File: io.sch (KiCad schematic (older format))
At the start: 7 parts, among them J3 Conn_02x05_Odd_Even, J4 Conn_02x10_Odd_Even, J5 Conn_02x05_Odd_Even, U10 TXB0104PW, U7 TXB0108DQSR, U8 TXB0108DQSR, U9 TXB0108DQSR

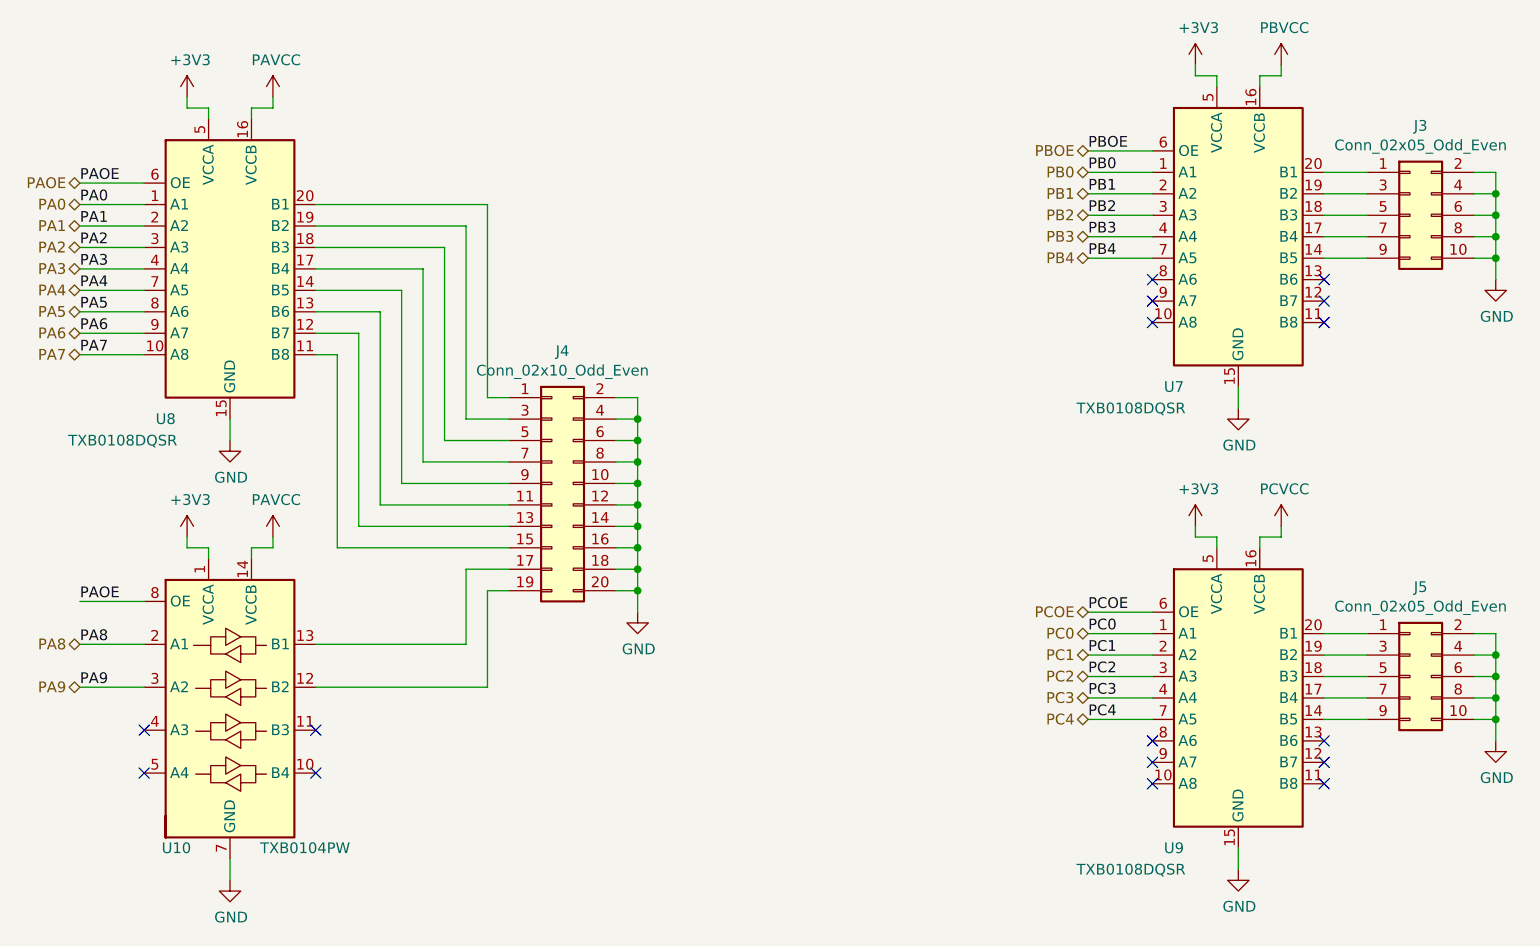
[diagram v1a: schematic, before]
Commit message: Routing should be done
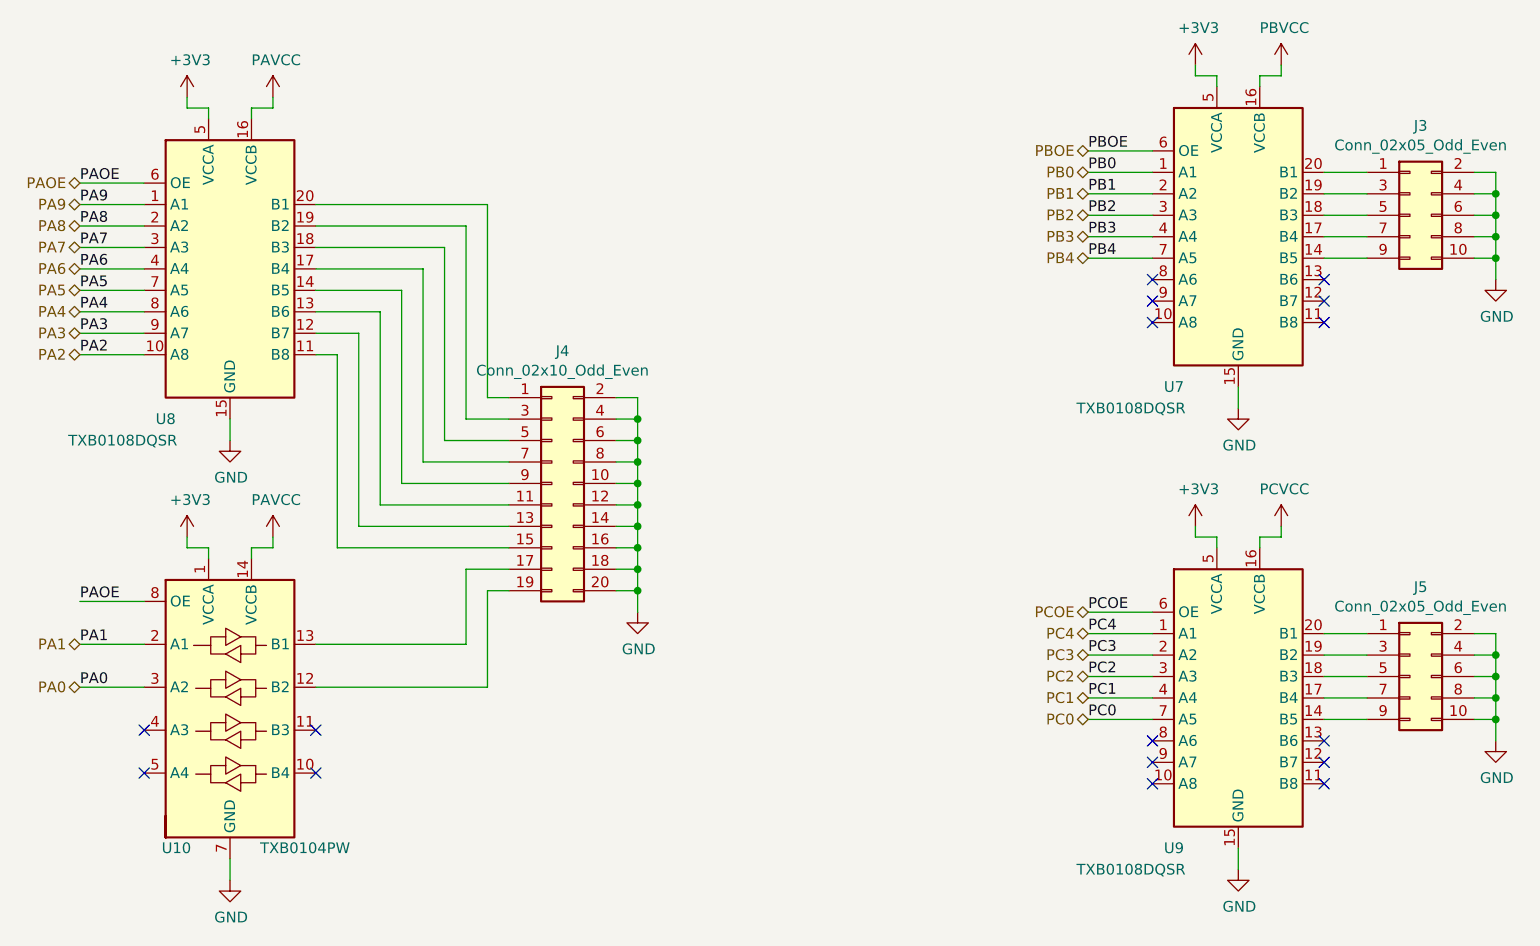
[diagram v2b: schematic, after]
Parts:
- U7, U8, U9: footprint Package_SON:USON-20_2x4mm_P0.4mm -> Package_SO:TSSOP-20_4.4x6.5mm_P0.65mm
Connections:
- net PA0: now also U10.3 (A2); no longer U8.1 (A1)
- net PA1: now also U10.2 (A1); no longer U8.2 (A2)
- net PA2: now also U8.10 (A8); no longer U8.3 (A3)
- net PA3: now also U8.9 (A7); no longer U8.4 (A4)
- net PA4: now also U8.8 (A6); no longer U8.7 (A5)
- net PA5: now also U8.7 (A5); no longer U8.8 (A6)
- net PA6: now also U8.4 (A4); no longer U8.9 (A7)
- net PA7: now also U8.3 (A3); no longer U8.10 (A8)
- net PA8: now also U8.2 (A2); no longer U10.2 (A1)
- net PA9: now also U8.1 (A1); no longer U10.3 (A2)
- net PC0: now also U9.7 (A5); no longer U9.1 (A1)
- net PC1: now also U9.4 (A4); no longer U9.2 (A2)
- net PC3: now also U9.2 (A2); no longer U9.4 (A4)
- net PC4: now also U9.1 (A1); no longer U9.7 (A5)
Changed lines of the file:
@@
-	1    0    0    -1
-$EndComp
-$Comp
-L Connector_Generic:Conn_02x10_Odd_Even J?
-U 1 1 5E95553C
-P 5300 3800
-AR Path="/5DFC2583/5E95553C" Ref="J?"  Part="1"
-AR Path="/5E933CA7/5E95553C" Ref="J4"  Part="1"
-F 0 "J4" H 5350 4417 50  0000 C CNN
-F 1 "Conn_02x10_Odd_Even" H 5350 4326 50  0000 C CNN
-F 2 "Connector_PinHeader_1.27mm:PinHeader_2x10_P1.27mm_Vertical_SMD" H 5300 3800 50  0001 C CNN
-F 3 "~" H 5300 3800 50  0001 C CNN
-	1    5300 3800
 	1    0    0    -1
 $EndComp
@@
 F 0 "U8" H 3500 2100 50  0000 C CNN
 F 1 "TXB0108DQSR" H 3300 2000 50  0000 C CNN
-F 2 "Package_SON:USON-20_2x4mm_P0.4mm" H 3800 2050 50  0001 C CNN
+F 2 "Package_SO:TSSOP-20_4.4x6.5mm_P0.65mm" H 3800 2050 50  0001 C CNN
 F 3 "http://www.ti.com/lit/ds/symlink/txb0108.pdf" H 3800 2700 50  0001 C CNN
 	1    3800 2800
@@
 F 0 "U9" H 8200 4100 50  0000 C CNN
 F 1 "TXB0108DQSR" H 8000 4000 50  0000 C CNN
-F 2 "Package_SON:USON-20_2x4mm_P0.4mm" H 8500 4050 50  0001 C CNN
+F 2 "Package_SO:TSSOP-20_4.4x6.5mm_P0.65mm" H 8500 4050 50  0001 C CNN
 F 3 "http://www.ti.com/lit/ds/symlink/txb0108.pdf" H 8500 4700 50  0001 C CNN
 	1    8500 4800
@@
 	1    0    0    -1
 $EndComp
-Text Label 3100 2500 0    50   ~ 0
+Text Label 3100 4750 0    50   ~ 0
 PA0
 Wire Wire Line
-	3400 2500 3100 2500
-Text Label 3100 2600 0    50   ~ 0
+	3400 4750 3100 4750
+Text Label 3100 4550 0    50   ~ 0
 PA1
 Wire Wire Line
-	3400 2600 3100 2600
+	3400 4550 3100 4550
+Text Label 3100 3200 0    50   ~ 0
+PA2
+Wire Wire Line
+	3400 3200 3100 3200
+Text Label 3100 3100 0    50   ~ 0
+PA3
+Wire Wire Line
+	3400 3100 3100 3100
+Text Label 3100 3000 0    50   ~ 0
+PA4
+Wire Wire Line
+	3400 3000 3100 3000
+Text Label 3100 2900 0    50   ~ 0
+PA5
+Wire Wire Line
+	3400 2900 3100 2900
+Text Label 3100 2800 0    50   ~ 0
+PA6
+Wire Wire Line
+	3400 2800 3100 2800
 Text Label 3100 2700 0    50   ~ 0
-PA2
+PA7
 Wire Wire Line
 	3400 2700 3100 2700
-Text Label 3100 2800 0    50   ~ 0
-PA3
-Wire Wire Line
-	3400 2800 3100 2800
-Text Label 3100 2900 0    50   ~ 0
-PA4
-Wire Wire Line
-	3400 2900 3100 2900
-Text Label 3100 3000 0    50   ~ 0
-PA5
-Wire Wire Line
-	3400 3000 3100 3000
-Text Label 3100 3100 0    50   ~ 0
-PA6
-Wire Wire Line
-	3400 3100 3100 3100
-Text Label 3100 3200 0    50   ~ 0
-PA7
-Wire Wire Line
-	3400 3200 3100 3200
 Text Label 3100 2400 0    50   ~ 0
 PAOE
 Wire Wire Line
 	3400 2400 3100 2400
-Text Label 3100 4550 0    50   ~ 0
+Text Label 3100 2600 0    50   ~ 0
 PA8
 Wire Wire Line
-	3400 4550 3100 4550
-Text Label 3100 4750 0    50   ~ 0
+	3400 2600 3100 2600
+Text Label 3100 2500 0    50   ~ 0
 PA9
 Wire Wire Line
-	3400 4750 3100 4750
+	3400 2500 3100 2500
 Text Label 3100 4350 0    50   ~ 0
 PAOE
@@
 F 0 "U7" H 8200 1950 50  0000 C CNN
 F 1 "TXB0108DQSR" H 8000 1850 50  0000 C CNN
-F 2 "Package_SON:USON-20_2x4mm_P0.4mm" H 8500 1900 50  0001 C CNN
+F 2 "Package_SO:TSSOP-20_4.4x6.5mm_P0.65mm" H 8500 1900 50  0001 C CNN
 F 3 "http://www.ti.com/lit/ds/symlink/txb0108.pdf" H 8500 2550 50  0001 C CNN
 	1    8500 2650
@@
 Wire Wire Line
 	8100 2250 7800 2250
-Text Label 7800 4500 0    50   ~ 0
+Text Label 7800 4900 0    50   ~ 0
 PC0
 Wire Wire Line
-	8100 4500 7800 4500
-Text Label 7800 4600 0    50   ~ 0
+	8100 4900 7800 4900
+Text Label 7800 4800 0    50   ~ 0
 PC1
 Wire Wire Line
-	8100 4600 7800 4600
+	8100 4800 7800 4800
 Text Label 7800 4700 0    50   ~ 0
 PC2
 Wire Wire Line
 	8100 4700 7800 4700
-Text Label 7800 4800 0    50   ~ 0
+Text Label 7800 4600 0    50   ~ 0
 PC3
 Wire Wire Line
-	8100 4800 7800 4800
-Text Label 7800 4900 0    50   ~ 0
+	8100 4600 7800 4600
+Text Label 7800 4500 0    50   ~ 0
 PC4
 Wire Wire Line
-	8100 4900 7800 4900
+	8100 4500 7800 4500
 Text Label 7800 4400 0    50   ~ 0
 PCOE
@@
 Text HLabel 3100 2400 0    50   BiDi ~ 0
 PAOE
+Text HLabel 3100 4750 0    50   BiDi ~ 0
+PA0
+Text HLabel 3100 4550 0    50   BiDi ~ 0
+PA1
+Text HLabel 3100 3200 0    50   BiDi ~ 0
+PA2
+Text HLabel 3100 3100 0    50   BiDi ~ 0
+PA3
+Text HLabel 3100 3000 0    50   BiDi ~ 0
+PA4
+Text HLabel 3100 2900 0    50   BiDi ~ 0
+PA5
+Text HLabel 3100 2800 0    50   BiDi ~ 0
+PA6
+Text HLabel 3100 2700 0    50   BiDi ~ 0
+PA7
+Text HLabel 3100 2600 0    50   BiDi ~ 0
+PA8
 Text HLabel 3100 2500 0    50   BiDi ~ 0
-PA0
-Text HLabel 3100 2600 0    50   BiDi ~ 0
-PA1
-Text HLabel 3100 2700 0    50   BiDi ~ 0
-PA2
-Text HLabel 3100 2800 0    50   BiDi ~ 0
-PA3
-Text HLabel 3100 2900 0    50   BiDi ~ 0
-PA4
-Text HLabel 3100 3000 0    50   BiDi ~ 0
-PA5
-Text HLabel 3100 3100 0    50   BiDi ~ 0
-PA6
-Text HLabel 3100 3200 0    50   BiDi ~ 0
-PA7
-Text HLabel 3100 4550 0    50   BiDi ~ 0
-PA8
-Text HLabel 3100 4750 0    50   BiDi ~ 0
 PA9
 Text HLabel 7800 2250 0    50   BiDi ~ 0
@@
 Text HLabel 7800 4400 0    50   BiDi ~ 0
 PCOE
-Text HLabel 7800 4500 0    50   BiDi ~ 0
+Text HLabel 7800 4900 0    50   BiDi ~ 0
 PC0
-Text HLabel 7800 4600 0    50   BiDi ~ 0
+Text HLabel 7800 4800 0    50   BiDi ~ 0
 PC1
 Text HLabel 7800 4700 0    50   BiDi ~ 0
 PC2
-Text HLabel 7800 4800 0    50   BiDi ~ 0
+Text HLabel 7800 4600 0    50   BiDi ~ 0
 PC3
-Text HLabel 7800 4900 0    50   BiDi ~ 0
+Text HLabel 7800 4500 0    50   BiDi ~ 0
 PC4
+$Comp
+L Connector_Generic:Conn_02x10_Odd_Even J?
+U 1 1 5E95553C
+P 5300 3800
+AR Path="/5DFC2583/5E95553C" Ref="J?"  Part="1"
+AR Path="/5E933CA7/5E95553C" Ref="J4"  Part="1"
+F 0 "J4" H 5350 4417 50  0000 C CNN
+F 1 "Conn_02x10_Odd_Even" H 5350 4326 50  0000 C CNN
+F 2 "Connector_PinHeader_1.27mm:PinHeader_2x10_P1.27mm_Vertical_SMD" H 5300 3800 50  0001 C CNN
+F 3 "~" H 5300 3800 50  0001 C CNN
+	1    5300 3800
+	1    0    0    -1
+$EndComp
 $EndSCHEMATC
